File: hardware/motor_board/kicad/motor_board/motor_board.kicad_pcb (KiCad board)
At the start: 4 copper layers, 75 x 35 mm, 237 parts, among them J1 BOOMELE_1.27-2x10P, J2 WAFER-SH1.0-6PWB, J3 WAFER-SH1.0-6PWB, J4 S5B-XH-A, Q1 HYG015N04LS1C2, Q2 HYG015N04LS1C2, Q3 HYG015N04LS1C2, Q4 HYG015N04LS1C2, Q5 HYG015N04LS1C2, Q6 HYG015N04LS1C2, Q7 HYG015N04LS1C2, Q8 HYG015N04LS1C2, U1 STM32G474RET6, U10 SN74LVC3G17DCUR, U11 TPS22945DCKR, U12 TPS22945DCKR, U13 LM74502DDFR, U14 74LVC1G17SE-7, U2 DRV8323RHRGZR, U3 DRV8316CRRGFR, U4 DRV8316CRRGFR, U5 AP2112K-3.3TRG1, U6 SN74LVC08APWR, U7 INA239AIDGSR, U8 BQ76907RGRR, U9 SN74LVC3G17DCUR

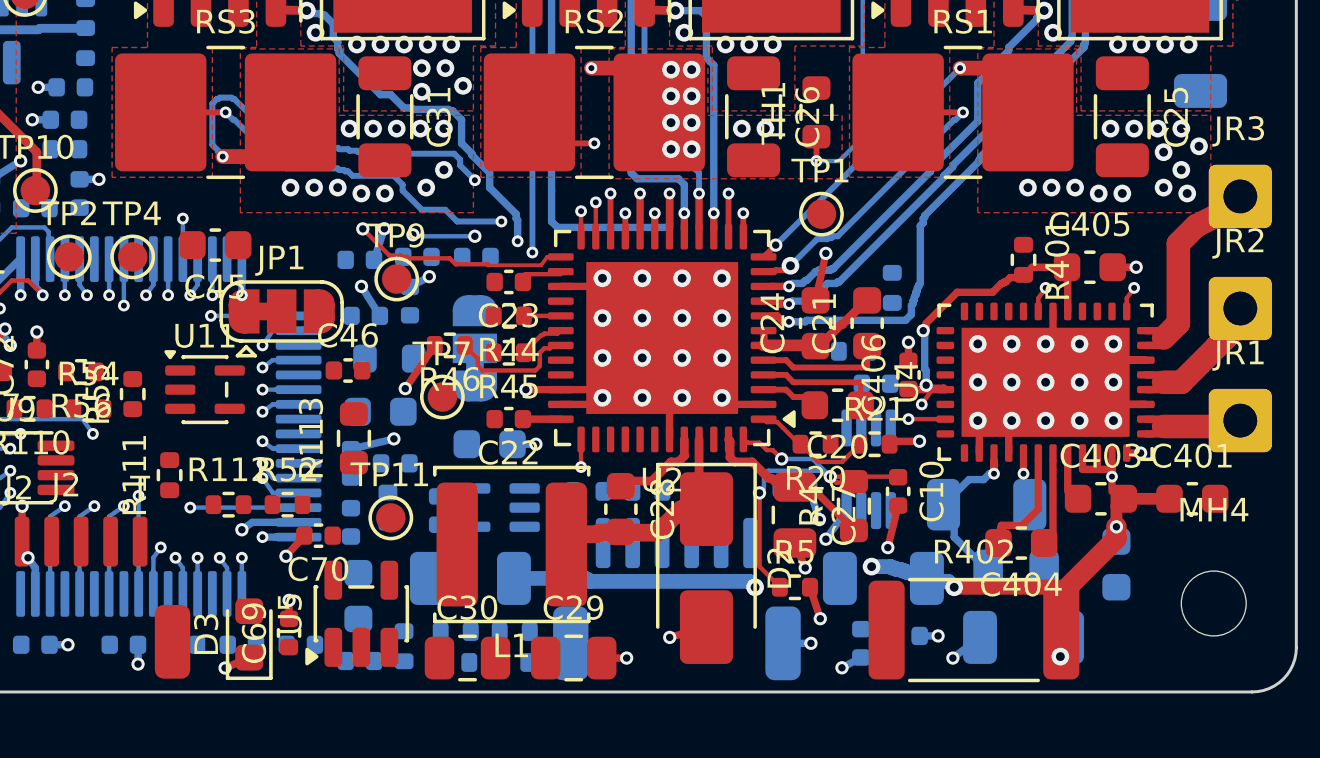
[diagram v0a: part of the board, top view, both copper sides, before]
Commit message: motor_board routing blocks 7c/7d: U4 escape (front row, left side; C405/R401 re-placed, C406 to the bottom) and U2 rear escape (C28 moved back, bootstrap re-drawn)
Co-Authored-By: Claude Opus 5.5 (1M context) <noreply@anthropic.com>
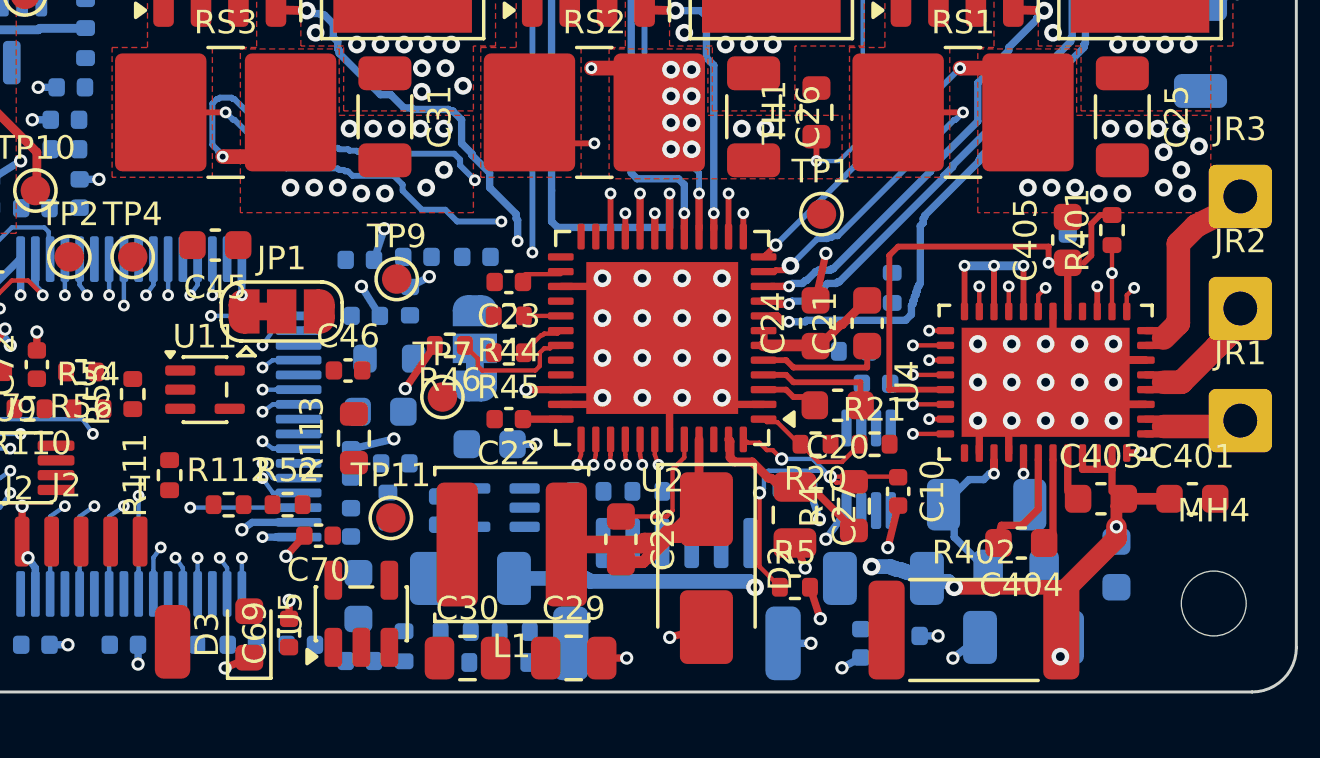
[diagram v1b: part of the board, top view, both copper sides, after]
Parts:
- C406: moved to B.Cu
- moved C406 6.89 mm to (167.2, 90.0)
- moved R401 3.17 mm to (168.8, 89.3), turned to 90 degrees
- moved C405 1.19 mm to (167.2, 89.7), turned to 90 degrees
- moved C28 1.03 mm to (152.1, 99.8)
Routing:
- net W_SOC: track 22.3 -> 1.22 mm, vias 2 -> 1
- net W_SOB: track 17.0 -> 1.31 mm, vias 4 -> 1
- net W_SOA: track 14.7 -> 0.00 mm, vias 2 -> 0
- net +3V3: track 37.7 -> 45.2 mm, vias 5 -> 9
- net /drive_right/R_AVDD: track 12.3 -> 17.4 mm, vias 3 -> 1
- net GND: track 92.2 -> 89.7 mm, vias 168 -> 165
- net R_nFAULT: track 1.22 -> 3.32 mm, vias 1 -> 2
- net SPI_MOSI: track 0.88 -> 1.98 mm, vias 1 -> 2
- net R_nCS: track 4.64 -> 5.74 mm, vias 1 -> 2
- net R_SOC: track 0.00 -> 1.10 mm, vias 0 -> 1
- net R_SOA: track 0.00 -> 1.10 mm, vias 0 -> 1
- net R_INHC: track 3.33 -> 4.17 mm, vias 1 -> 2
- net R_INHB: track 1.31 -> 2.16 mm, vias 1 -> 2
- net /drive_right/R_VM: track 28.8 -> 28.0 mm, vias 6 -> 5
- net /weapon/W_INLC: track 0.00 -> 0.72 mm, vias 0 -> 1
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
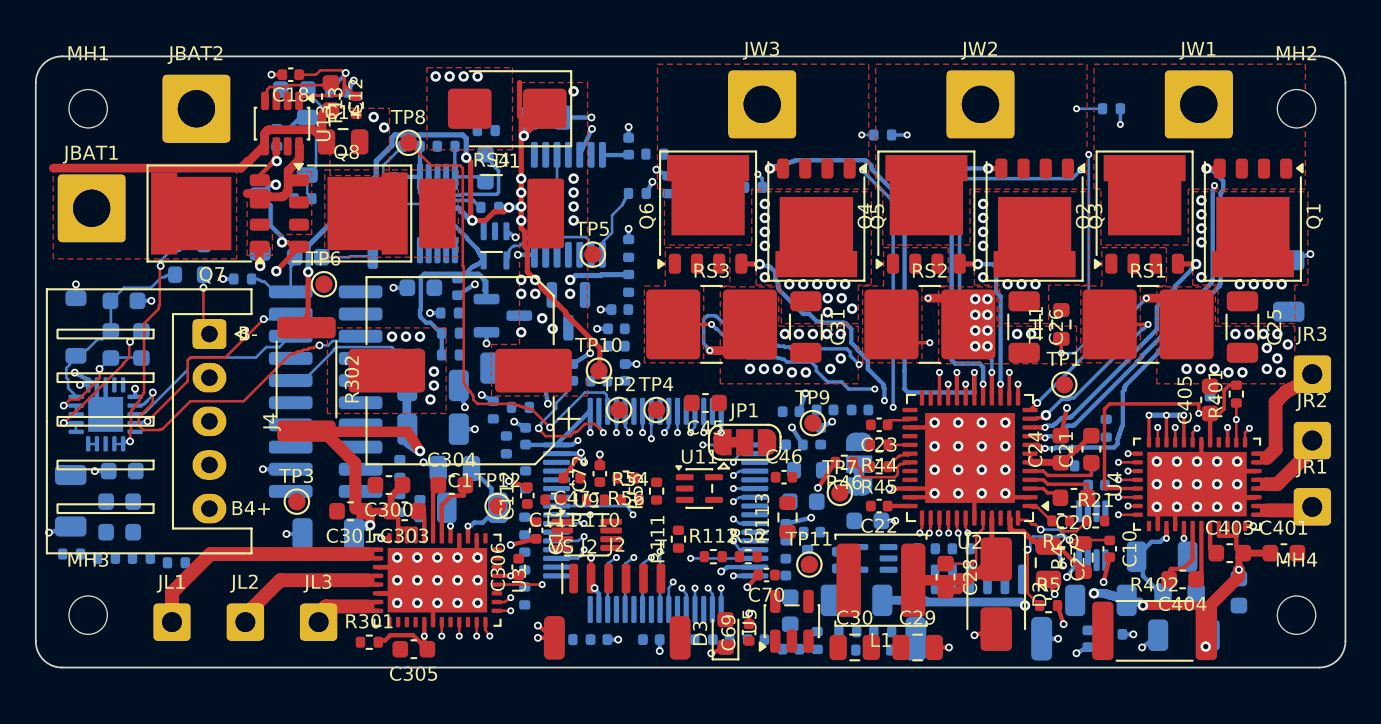
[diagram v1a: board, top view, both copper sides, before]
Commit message: motor_board routing block 8: east bus (L3) complete U1<->U4
Twelve planned L3 lanes behind U2; U4 front group round U1's NE corner into its
top-row vias, INHA/INHC through the right-column gap, south group round U1's rear.
CSA filters R80/R81 moved to the top at U4's corner and R82 beside U1.25
(they sat west of U1, the wrong side for both ends); C90/C91 swapped so the
outer lanes drop straight into them. nCS hops once on top between J2's pins.
Router gains a per-request tol. DRC 0, 285 unconnected.

Co-Authored-By: Claude Opus 5.5 (1M context) <noreply@anthropic.com>
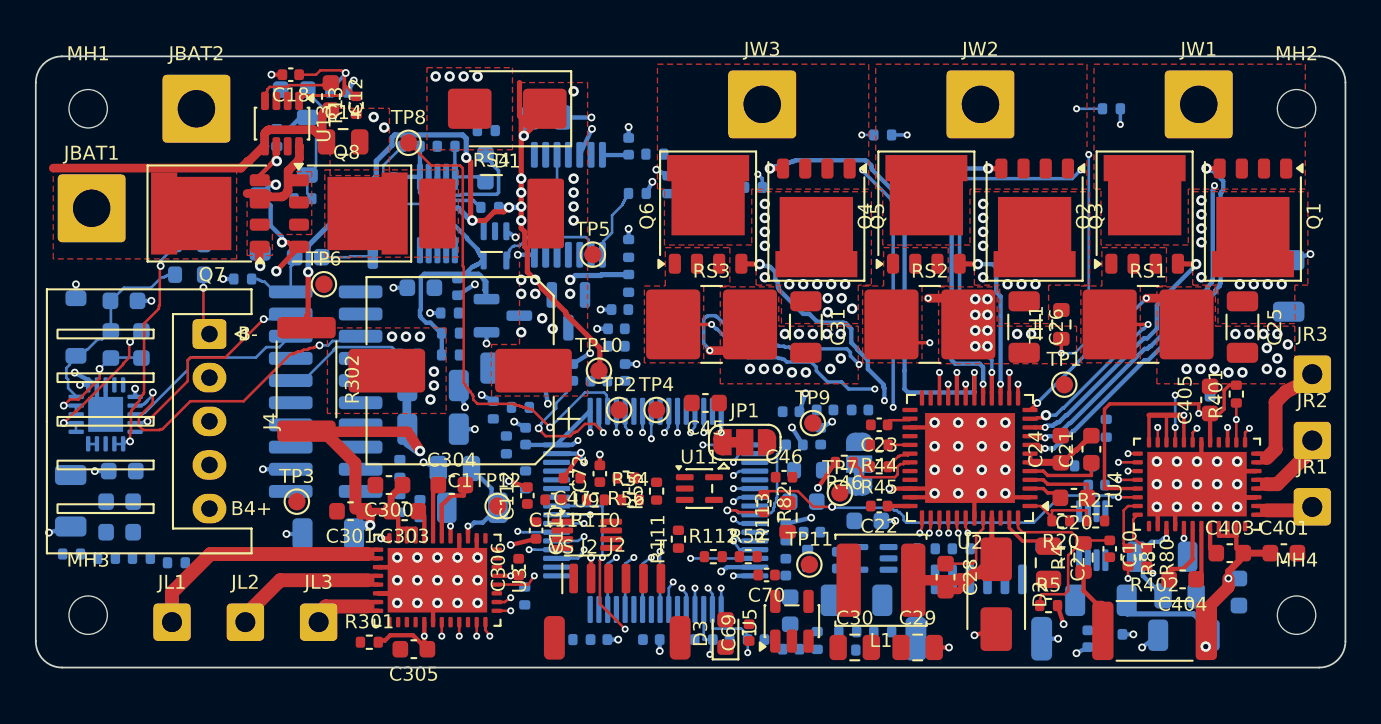
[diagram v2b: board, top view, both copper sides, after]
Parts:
- R80, R81, R82: moved to F.Cu
- moved R80 35.6 mm to (163.6, 98.7)
- moved R81 34.6 mm to (162.6, 98.7)
- moved R82 10.8 mm to (141.7, 95.6), turned to -90 degrees
- moved C90 2.00 mm to (141.2, 103.4)
- moved C91 2.00 mm to (139.2, 103.4)
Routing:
- net DRV_OFF: track 28.2 -> 88.1 mm
- net R_nFAULT: track 3.32 -> 57.9 mm
- net SPI_MOSI: track 1.98 -> 52.3 mm, vias 2 -> 3
- net SPI_SCK: track 0.55 -> 49.1 mm, vias 1 -> 2
- net R_INHB: track 2.16 -> 50.0 mm, vias 2 -> 3
- net SPI_MISO: track 3.01 -> 46.3 mm
- net R_nCS: track 5.74 -> 48.2 mm, vias 2 -> 3
- net R_INHA: track 2.21 -> 41.6 mm
- net R_INHC: track 4.17 -> 42.8 mm
- net /mcu/R_SOA_F: track 1.31 -> 33.9 mm, vias 1 -> 3
- net /mcu/R_SOB_F: track 0.00 -> 32.1 mm, vias 0 -> 2
- net R_SOC: track 1.10 -> 23.0 mm, vias 1 -> 2
- net /drive_right/R_VM: track 28.0 -> 13.9 mm, vias 5 -> 2
- net GND: track 89.7 -> 77.1 mm, vias 165 -> 153
- net /mcu/R_SOC_F: track 0.00 -> 9.10 mm, vias 0 -> 1
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
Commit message: motor_board routing block 9a: BMS corner (U8/J4/R7-R11/C4-C11), router with frozen pairs; DRC 0
Co-Authored-By: Claude Opus 5.5 (1M context) <noreply@anthropic.com>
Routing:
- net W_SOC: track 1.22 -> 26.4 mm, vias 1 -> 3
- net W_SOB: track 1.31 -> 17.0 mm, vias 1 -> 5
- net W_SOA: track 0.00 -> 14.7 mm, vias 0 -> 2
- net /power/BAL1: track 0.00 -> 13.5 mm, vias 0 -> 3
- net /power/CELL2: track 8.37 -> 19.4 mm
- net /power/BAL2: track 0.00 -> 10.4 mm, vias 0 -> 1
- net /power/CELL1: track 7.12 -> 17.0 mm, vias 2 -> 4
- net /power/CELL3: track 0.50 -> 8.87 mm, vias 0 -> 2
- net /power/BAL3: track 0.00 -> 7.95 mm, vias 0 -> 1
- net /power/CELL4: track 0.00 -> 4.39 mm, vias 0 -> 2
- net /power/BAL4: track 0.00 -> 3.67 mm, vias 0 -> 1
- net /power/BMS_BAT: track 13.3 -> 16.8 mm
- net /power/BMS_REG: track 0.00 -> 2.40 mm

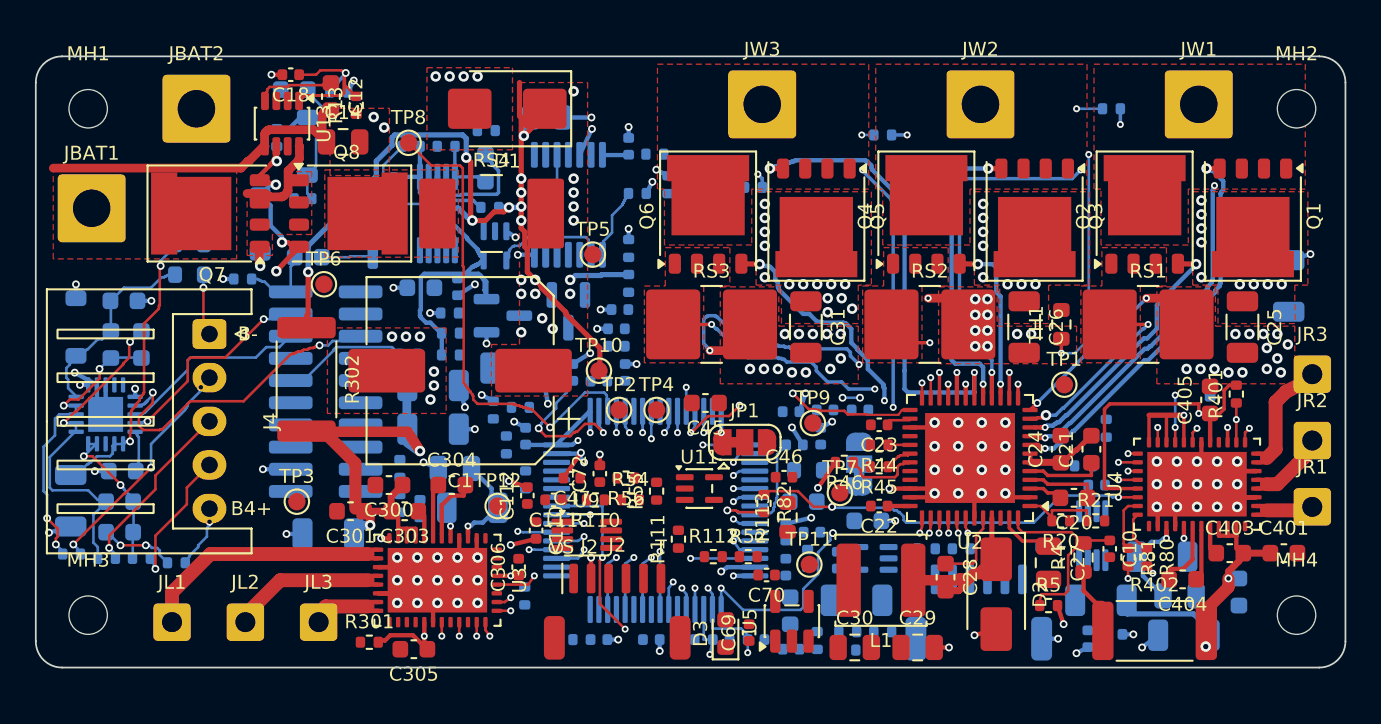
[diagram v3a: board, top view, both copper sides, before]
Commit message: motor_board routing block 11a: NW bottom-side logic, local pairs; router avoid boxes; spot.py; plan status
Co-Authored-By: Claude Opus 5.5 (1M context) <noreply@anthropic.com>
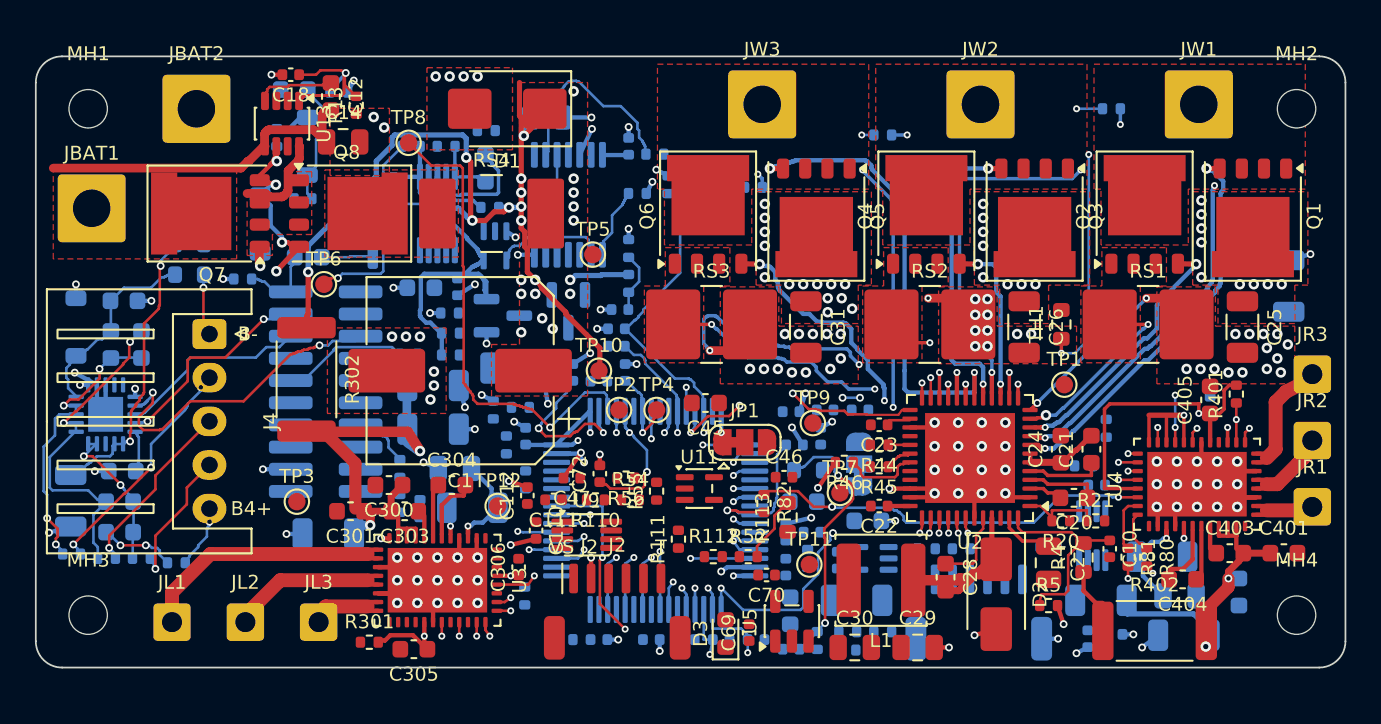
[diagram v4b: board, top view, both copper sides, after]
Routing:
- net W_VC: track 1.22 -> 21.0 mm
- net R_MTEMP: track 0.00 -> 15.4 mm, vias 0 -> 2
- net W_INLC_M: track 1.31 -> 13.0 mm
- net L_MTEMP: track 1.31 -> 11.9 mm, vias 1 -> 2
- net /mcu/NRST: track 1.22 -> 9.67 mm
- net /weapon/W_ARM: track 0.00 -> 6.60 mm, vias 0 -> 1
- net /mcu/L_SOC_F: track 1.22 -> 6.44 mm
- net /mcu/VBAT_SNS: track 2.98 -> 6.47 mm

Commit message: motor_board routing: feasibility trials (west, nw, hard) behind TRIAL=; plan status: U2 region enclosed on 4 layers
Co-Authored-By: Claude Opus 5.5 (1M context) <noreply@anthropic.com>
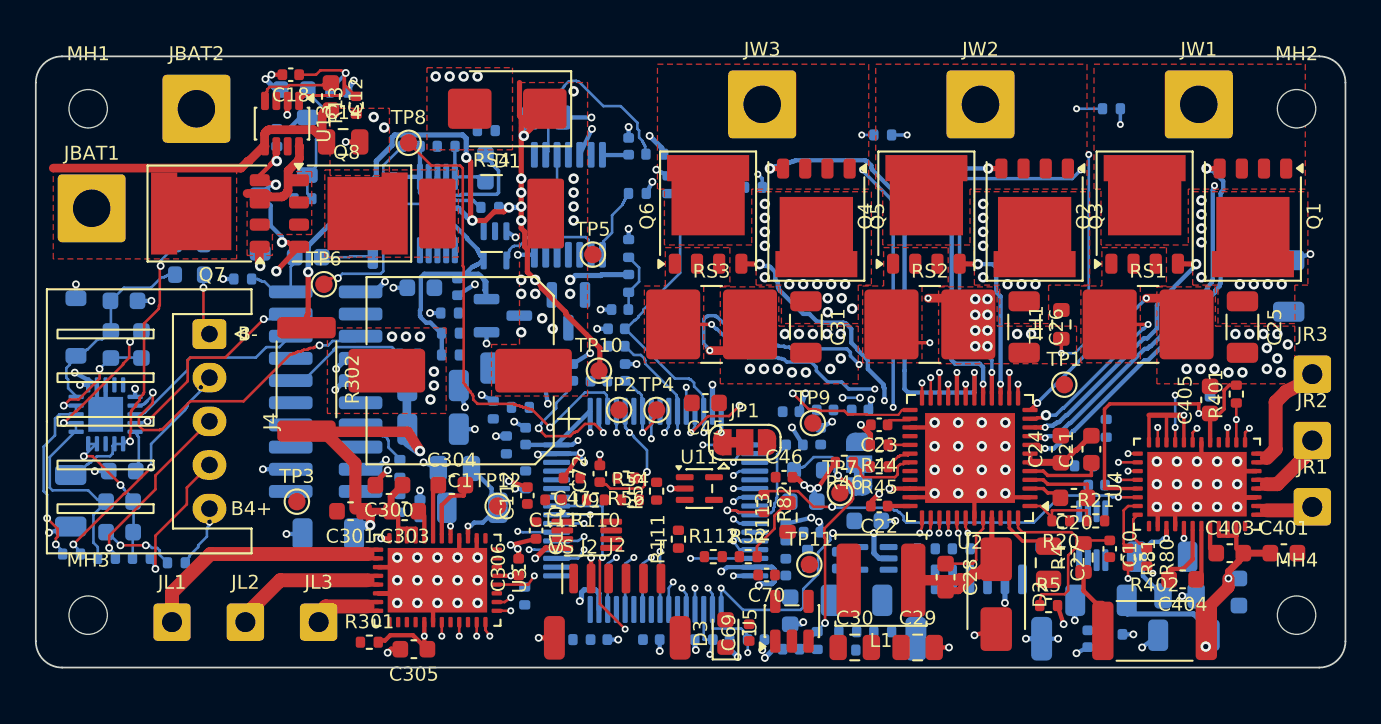
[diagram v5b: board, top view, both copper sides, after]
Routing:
- net GND: track 77.1 -> 119.9 mm, vias 153 -> 190

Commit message: motor_board: go to 6 layers (F / L2 GND / L3 VBAT feed + lanes / L4 signals / L5 GND / B)
Base edit sets 6 copper layers, adds the L5 GND plane (copy of L2's), writes a 1.6 mm
1 oz stack-up; router, geo, geom_export, apply_routes, layout_check know In3/In4.
Everything routed keeps its layer. DRC 0, 220 unconnected.

Co-Authored-By: Claude Opus 5.5 (1M context) <noreply@anthropic.com>
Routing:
- added copper zone on In4.Cu, net GND
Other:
- copper layers 4 -> 6
